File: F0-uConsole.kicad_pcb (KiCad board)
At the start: 2 copper layers, 54.7 x 77 mm, 7 parts, among them J1 uConsoleEXT, J2 F0_1, J3 F0_2, J4 USB1, J5 USB2

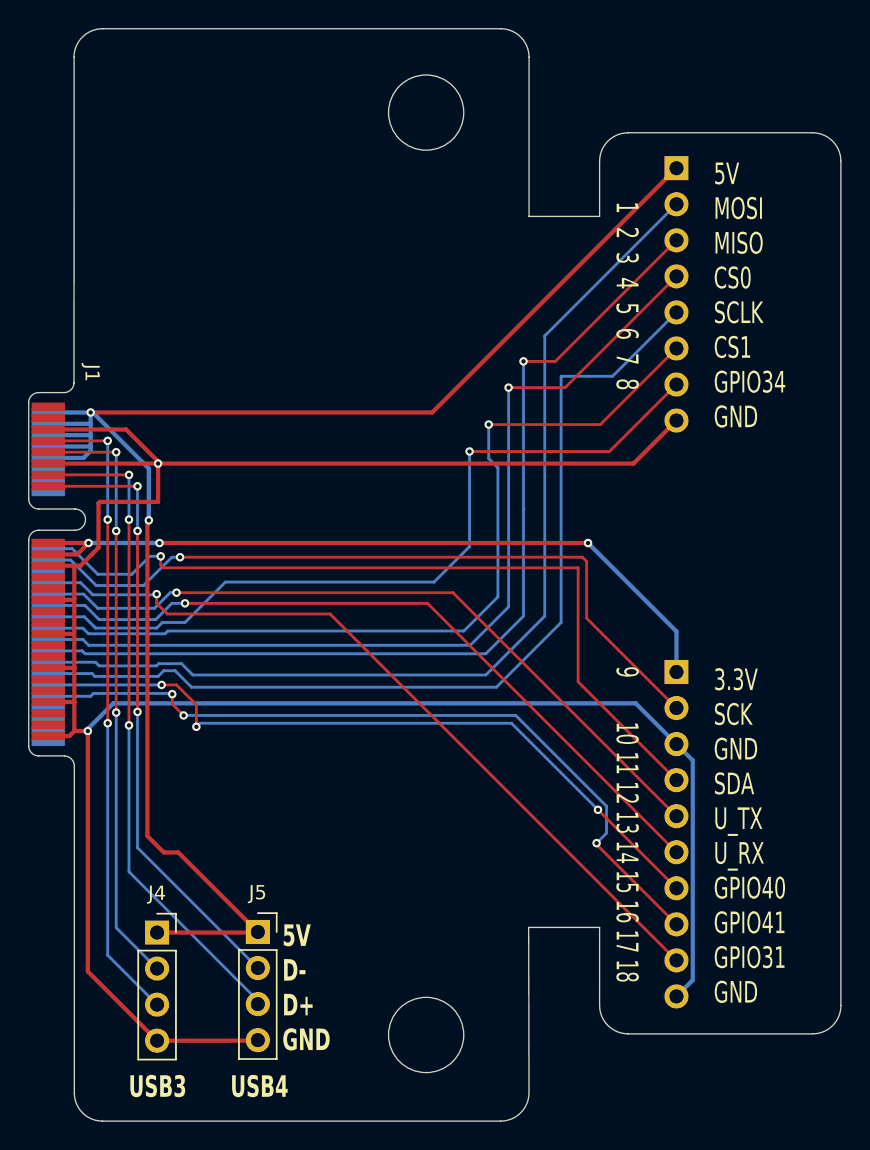
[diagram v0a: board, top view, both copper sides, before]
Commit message: Upload Rev0.2 board
change notes: 
added speaker terminals
flipped the flipper connector so the module face would be facing the user. basically this meant a full redesign.
shortened the card slightly.
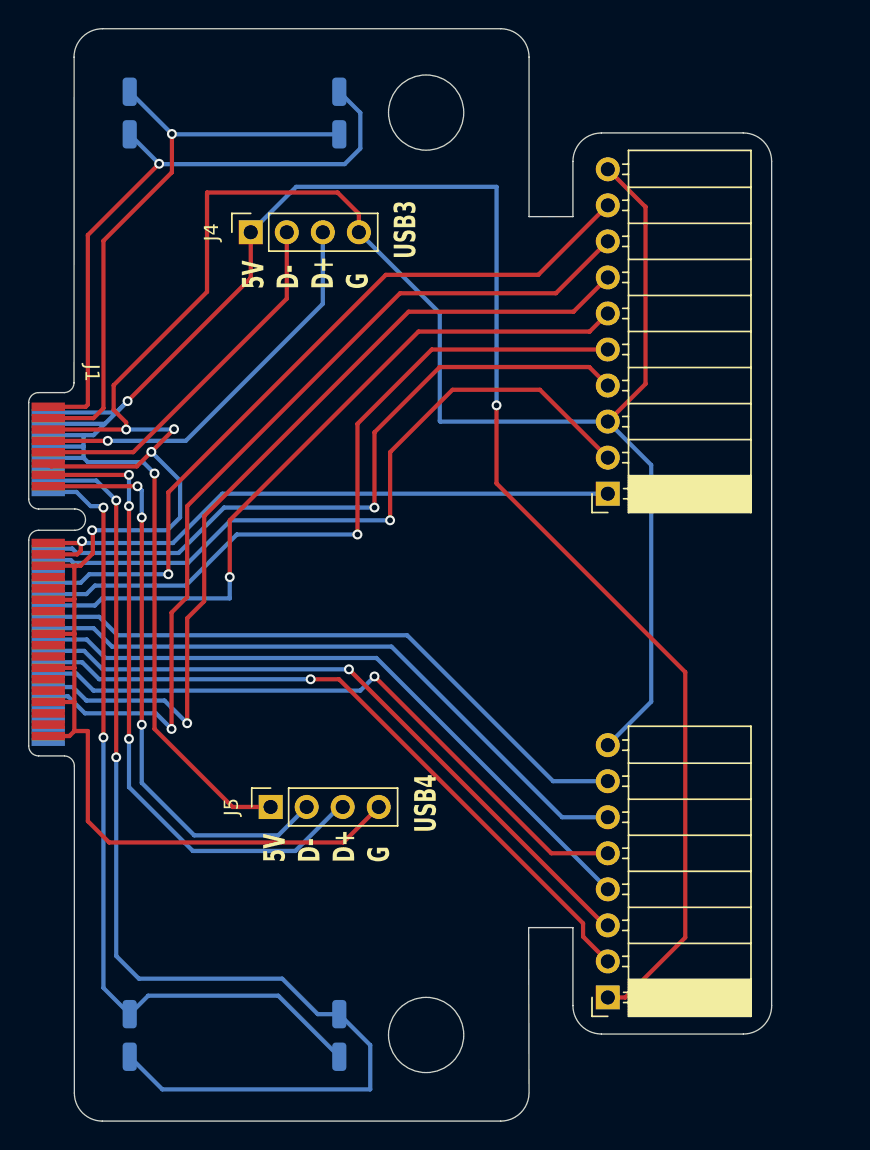
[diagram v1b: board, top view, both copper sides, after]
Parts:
- added U2: Speaker, uconsole:speaker pads, B.Cu at (117.1, 109.5)
- added U3: Speaker, uconsole:speaker pads, B.Cu at (117.1, 44.5)
- J2, J3: moved to F.Cu
- moved J2 58.6 mm to (143.4, 106.8)
- moved J4 49.8 mm to (118.3, 52.9), turned to 90 degrees
- moved J3 13.5 mm to (143.4, 71.3)
- moved J5 8.86 mm to (119.7, 93.4), turned to 90 degrees
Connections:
- J1 pad 1: unconnected-(J1-SPK_LP-Pad1) -> /SPK_LP
- J1 pad 14: unconnected-(J1-SPK_RP-Pad14) -> /SPK_RP
- J1 pad 16: unconnected-(J1-SPK_RN-Pad16) -> /SPK_RN
- J1 pad 3: unconnected-(J1-SPK_LN-Pad3) -> /SPK_LN
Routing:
- net /SPK_RP: track 0.00 -> 79.0 mm, vias 0 -> 2
- net /SPK_RN: track 0.00 -> 57.9 mm, vias 0 -> 2
- net /SPK_LP: track 0.00 -> 44.1 mm, vias 0 -> 1
- net /SPK_LN: track 0.00 -> 41.5 mm, vias 0 -> 1
- net +5V: track 115.7 -> 156.8 mm, vias 2 -> 3
- net SPI_MOSI: track 70.1 -> 48.7 mm, vias 0 -> 1
- net SPI_SCLK: track 66.1 -> 45.5 mm, vias 0 -> 1
- net SPI_MISO: track 67.2 -> 47.5 mm
- net SPI_CE0: track 64.4 -> 46.7 mm, vias 1 -> 0
- net USB3_DP: track 45.4 -> 28.4 mm, vias 3 -> 1
- net USB3_DN: track 42.4 -> 26.0 mm, vias 3 -> 0
- net SPI_CE1: track 60.8 -> 45.0 mm, vias 1 -> 0
- net GPIO34: track 55.6 -> 44.2 mm, vias 1 -> 0
- net GPIO40: track 51.4 -> 61.4 mm, vias 3 -> 1
- net GPIO41: track 54.2 -> 63.2 mm, vias 3 -> 1
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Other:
- board size 54.7 x 77 mm -> 49.9 x 77 mm
- board text added: "5V D- D+ G"
- board text removed: "5V D- D+ GND"
- board text removed: "uConsole to FlipperZero Module Hacked together by Timmotools"

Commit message: upload Rev0.2
forgot the revision on the silkscreen.
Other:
- board text added: "uConsole to Flipper0 module adaptor board Hacked together by Timmotools Rev 0.2"
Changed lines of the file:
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@@
+		)
+	)
+	(gr_text "uConsole to Flipper0\nmodule adaptor board\nHacked together by Timmotools\nRev 0.2"
+		(at 127.5 74.4 90)
+		(layer "F.SilkS")
+		(effects
+			(font
+				(size 1.52 1)
+				(thickness 0.25)
+				(bold yes)
+			)
+			(justify bottom)
 		)
 	)
